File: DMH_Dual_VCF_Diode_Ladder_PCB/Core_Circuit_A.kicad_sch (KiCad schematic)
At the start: 53 parts, among them SW1 SW_SPDT, SW2 SW_SPDT, SW3 SW_SPDT, SW5 Switch_SP3T_APEM5244, U1 TL074, U2 TL074

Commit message: Schematic design in progress
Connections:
- net GND: no longer SW5.3

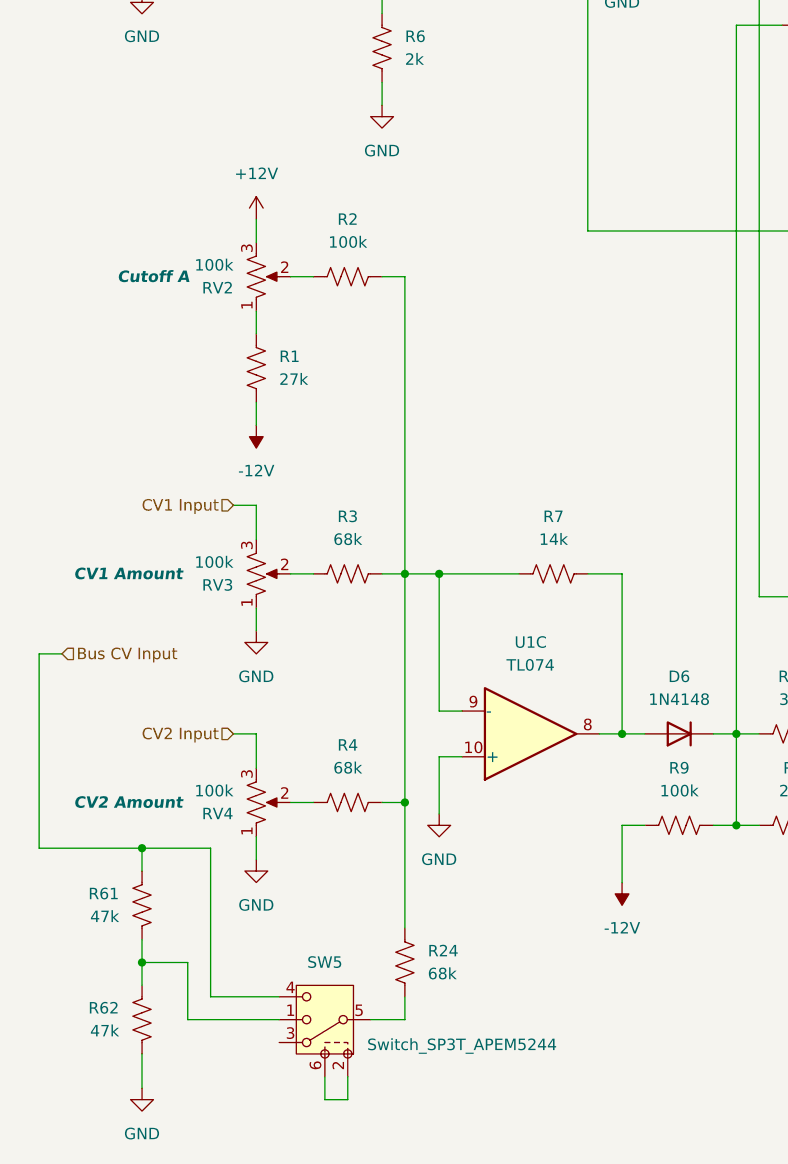
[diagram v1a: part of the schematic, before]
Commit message: Made CV processing page
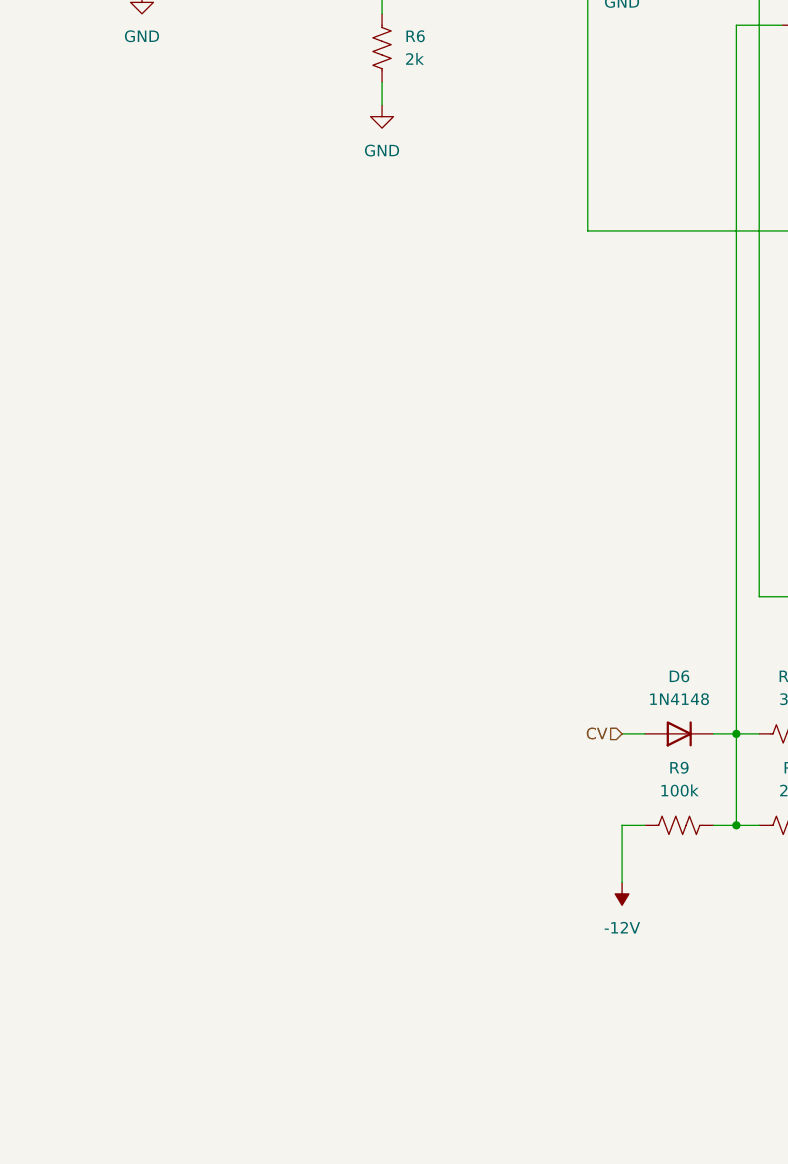
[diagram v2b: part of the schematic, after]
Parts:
- removed R1: 27k, Resistor_THT:R_Axial_DIN0207_L6.3mm_D2.5mm_P7.62mm_Horizontal, symbol Device:R_US
- removed R2: 100k, Resistor_THT:R_Axial_DIN0207_L6.3mm_D2.5mm_P7.62mm_Horizontal, symbol Device:R_US
- removed R24, R3, R4: 68k, Resistor_THT:R_Axial_DIN0207_L6.3mm_D2.5mm_P7.62mm_Horizontal, symbol Device:R_US
- removed R61, R62: 47k, Resistor_THT:R_Axial_DIN0207_L6.3mm_D2.5mm_P7.62mm_Horizontal, symbol Device:R_US
- removed R7: 14k, Resistor_THT:R_Axial_DIN0207_L6.3mm_D2.5mm_P7.62mm_Horizontal, symbol Device:R_US
- removed RV2: 100k, SynthStuff:Potentiometer_Alpha_RD901F-40-00D_Single_Vertical, symbol Device:R_Potentiometer_US
- removed RV3, RV4: 100k, SynthStuff:Potentiometer_TT_P110KH1, symbol Device:R_Potentiometer_US
- removed SW5: Switch_SP3T_APEM5244, symbol SynthStuff:Switch_SP3T
- removed unit 3 of U1
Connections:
- net CV: now reaches D6.2 (A)

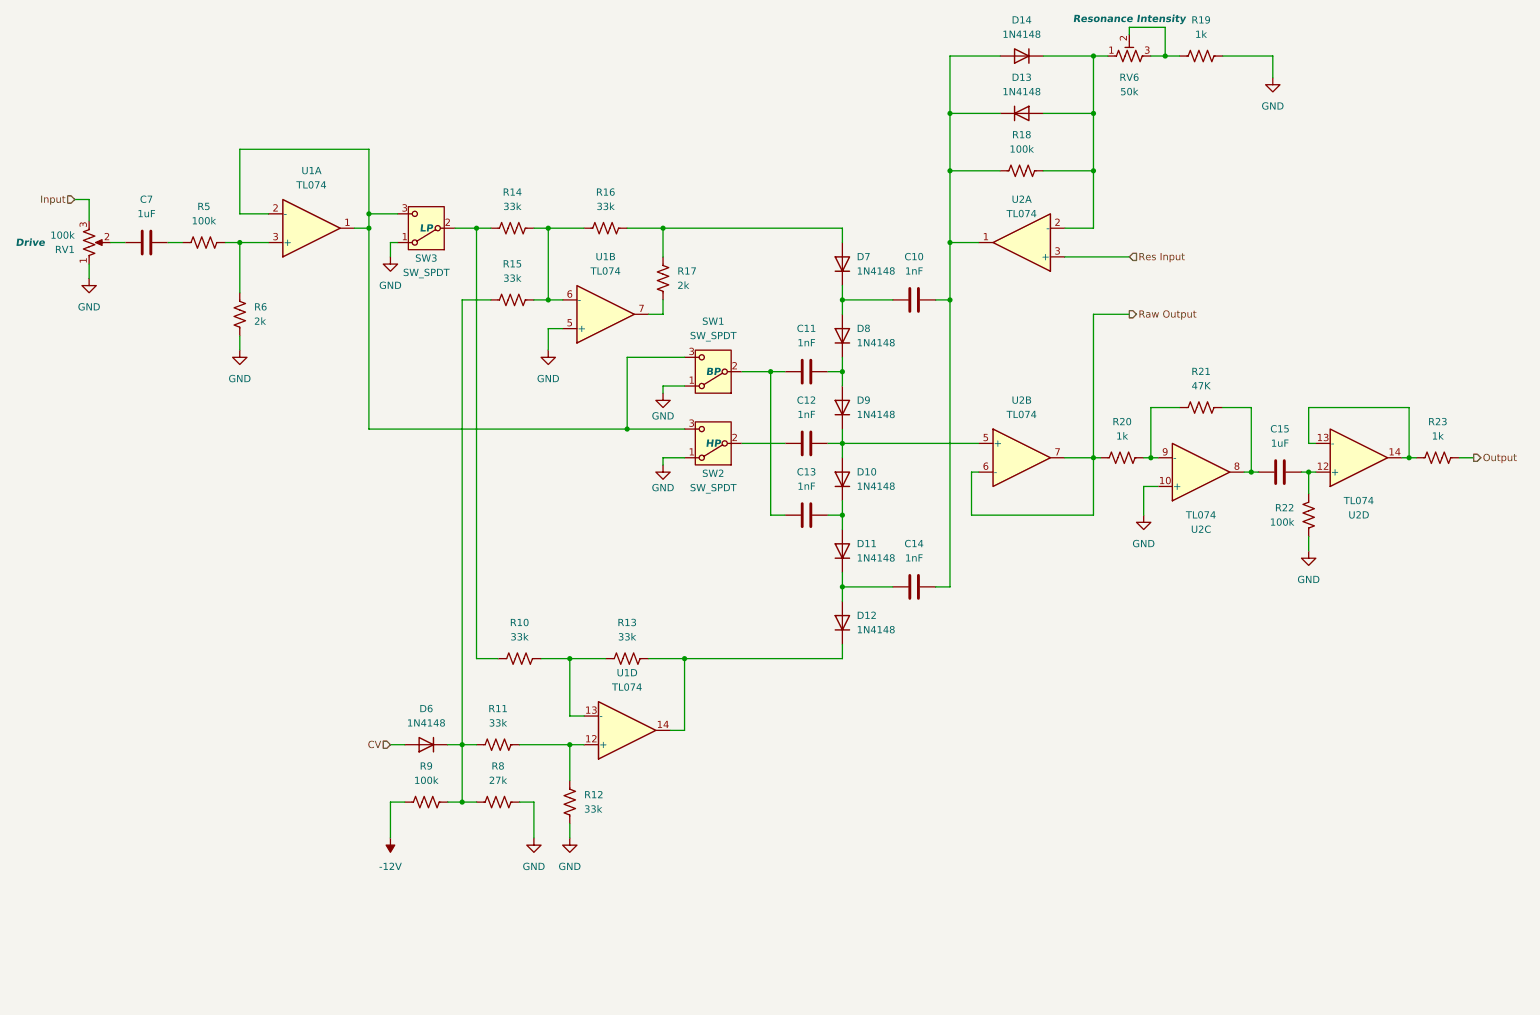
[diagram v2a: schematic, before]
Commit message: Reannotated whole schematic
OpAmp annotation is still tentative.
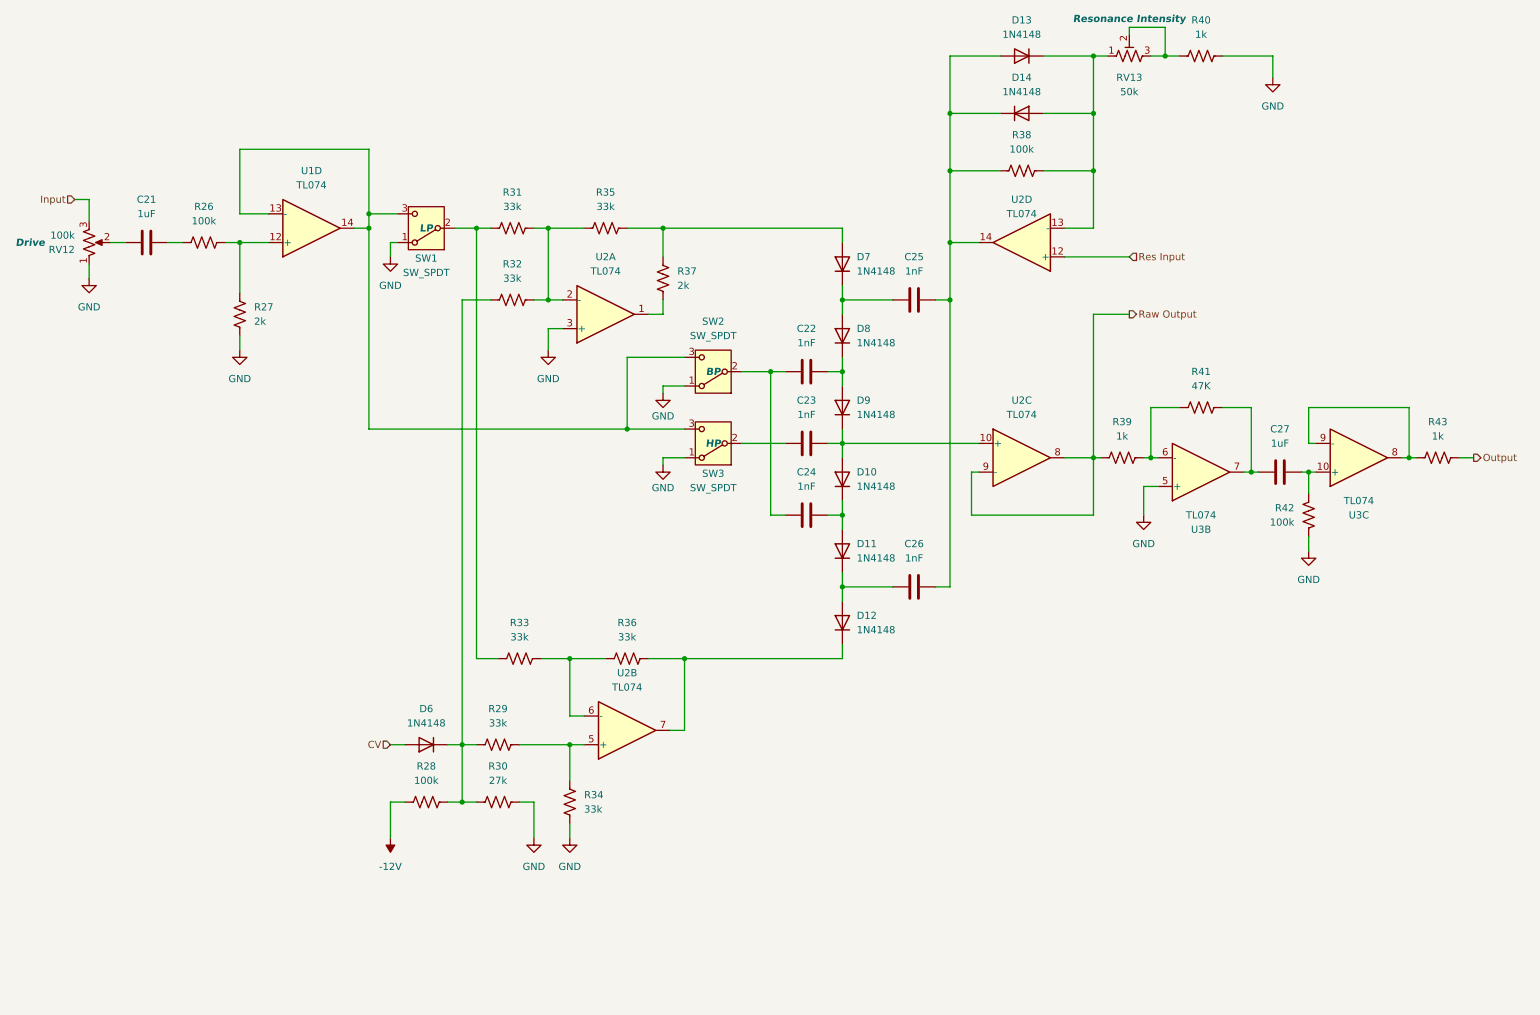
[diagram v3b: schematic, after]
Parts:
- removed C10, C11, C12, C13, C14: 1nF, Capacitor_THT:C_Disc_D4.3mm_W1.9mm_P5.00mm, symbol Device:C
- removed C15, C7: 1uF, Capacitor_THT:C_Disc_D4.3mm_W1.9mm_P5.00mm, symbol Device:C
- removed R10, R11, R12, R13, R14, R15, R16: 33k, Resistor_THT:R_Axial_DIN0207_L6.3mm_D2.5mm_P7.62mm_Horizontal, symbol Device:R_US
- removed R17, R6: 2k, Resistor_THT:R_Axial_DIN0207_L6.3mm_D2.5mm_P7.62mm_Horizontal, symbol Device:R_US
- removed R18, R22, R5, R9: 100k, Resistor_THT:R_Axial_DIN0207_L6.3mm_D2.5mm_P7.62mm_Horizontal, symbol Device:R_US
- removed R19, R20, R23: 1k, Resistor_THT:R_Axial_DIN0207_L6.3mm_D2.5mm_P7.62mm_Horizontal, symbol Device:R_US
- removed R21: 47K, Resistor_THT:R_Axial_DIN0207_L6.3mm_D2.5mm_P7.62mm_Horizontal, symbol Device:R_US
- removed R8: 27k, Resistor_THT:R_Axial_DIN0207_L6.3mm_D2.5mm_P7.62mm_Horizontal, symbol Device:R_US
- removed RV1: 100k, SynthStuff:Potentiometer_Alpha_RD901F-40-00D_Single_Vertical, symbol Device:R_Potentiometer_US
- removed RV6: 50k, Potentiometer_THT:Potentiometer_Bourns_3296W_Vertical, symbol Device:R_Potentiometer_Trim_US
- removed unit 2 of U1
- removed unit 1 of U1
- added C21, C27: 1uF, Capacitor_THT:C_Disc_D4.3mm_W1.9mm_P5.00mm, symbol Device:C
- added C22, C23, C24, C25, C26: 1nF, Capacitor_THT:C_Disc_D4.3mm_W1.9mm_P5.00mm, symbol Device:C
- added R26, R28, R38, R42: 100k, Resistor_THT:R_Axial_DIN0207_L6.3mm_D2.5mm_P7.62mm_Horizontal, symbol Device:R_US
- added R27, R37: 2k, Resistor_THT:R_Axial_DIN0207_L6.3mm_D2.5mm_P7.62mm_Horizontal, symbol Device:R_US
- added R29, R31, R32, R33, R34, R35, R36: 33k, Resistor_THT:R_Axial_DIN0207_L6.3mm_D2.5mm_P7.62mm_Horizontal, symbol Device:R_US
- added R30: 27k, Resistor_THT:R_Axial_DIN0207_L6.3mm_D2.5mm_P7.62mm_Horizontal, symbol Device:R_US
- added R39, R40, R43: 1k, Resistor_THT:R_Axial_DIN0207_L6.3mm_D2.5mm_P7.62mm_Horizontal, symbol Device:R_US
- added R41: 47K, Resistor_THT:R_Axial_DIN0207_L6.3mm_D2.5mm_P7.62mm_Horizontal, symbol Device:R_US
- added RV12: 100k, SynthStuff:Potentiometer_Alpha_RD901F-40-00D_Single_Vertical, symbol Device:R_Potentiometer_US
- added RV13: 50k, Potentiometer_THT:Potentiometer_Bourns_3296W_Vertical, symbol Device:R_Potentiometer_Trim_US
- added U3: TL074, Package_DIP:DIP-14_W7.62mm_Socket, symbol Amplifier_Operational:TL074
- SW1: Function BP -> LP
- SW2: Function HP -> BP
- SW3: Function LP -> HP
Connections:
- net -12V: now also R28.1
- net GND: now also U2.3 (+), R27.1, R30.2, R34.1, R40.2, R42.1, RV12.1, U3.5 (+); no longer U2.10 (+)
- net Input: now also RV12.3
- net Output: now also R43.2
- net Raw Output: now also U2.8, U2.9 (-), R39.1; no longer U2.6 (-), U2.7
- net Res Input: now also U2.12 (+); no longer U2.3 (+)
- net at D6.1 (K): now also R28.2, R29.1, R30.1, R32.1
- net at SW2.2 (B): now also C22.1, C24.1
- net at D10.2 (A), D9.1 (K): now also U2.10 (+), C23.2; no longer U2.5 (+)
- net at D7.2 (A): now also R35.2, R37.2
- net at SW1.2 (B): now also R31.1, R33.1
- net at D10.1 (K), D11.2 (A): now also C24.2
- net at D8.1 (K), D9.2 (A): now also C22.2
- net at SW1.3 (C), SW2.3 (C), SW3.3 (C): now also U1.13 (-), U1.14
- net at D7.1 (K), D8.2 (A): now also C25.1
- net at D13.1 (K), D14.2 (A): now also U2.13 (-), R38.2, RV13.1; no longer U2.1
- net at D13.2 (A), D14.1 (K): now also U2.14, C25.2, C26.2, R38.1; no longer U2.2 (-)
- net at SW3.2 (B): now also C23.1
- net at U1.12 (+): now also R26.2, R27.2
- net at D11.1 (K), D12.2 (A): now also C26.1
- net at D12.1 (K): now also U2.7, R36.2; no longer U1.14
- new net: C21.1, RV12.2
- new net: C27.2, R42.2, U3.10 (+)
- new net: R43.1, U3.8, U3.9 (-)
- new net: C27.1, R41.2, U3.7
- new net: R39.2, R41.1, U3.6 (-)
- new net: R31.2, R32.2, R35.1, U2.2 (-)
- new net: R37.1, U2.1
- new net: R29.2, R34.2, U2.5 (+)
- new net: C21.2, R26.1
- new net: R40.1, RV13.2, RV13.3
- new net: R33.2, R36.1, U2.6 (-)

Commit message: Reannotated OpAmps and cleared errors
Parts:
- renumbered U2 to U3, U3 to U4, U2 to U4
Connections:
- net GND: now also U4.3 (+); no longer U4.5 (+)
- net at C27.2, R42.2: now also U3.5 (+); no longer U3.10 (+)
- net at C27.1, R41.2: now also U4.1; no longer U4.7
- net at R39.2, R41.1: now also U4.2 (-); no longer U4.6 (-)
- new net: R43.1, U3.6 (-), U3.7
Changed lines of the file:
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@@
 		(at 250.19 101.6 0)
 		(mirror x)
-		(unit 3)
+		(unit 2)
 		(exclude_from_sim no)
 		(in_bom yes)
@@
 				(path "/58f4306d-5387-4983-bb08-41a2313fd315/7ad2d702-dfb7-4d49-a82d-34430dd5948f"
 					(reference "U3")
-					(unit 3)
+					(unit 2)
 				)
 			)
@@
 		(at 222.25 104.14 0)
 		(mirror x)
-		(unit 2)
+		(unit 1)
 		(exclude_from_sim no)
 		(in_bom yes)
 		(on_board yes)
 		(dnp no)
-		(property "Reference" "U3"
+		(property "Reference" "U4"
 			(at 222.25 114.3 0)
 			(effects
@@
 			(project "DMH_Dual_VCF_Diode_Ladder_PCB"
 				(path "/58f4306d-5387-4983-bb08-41a2313fd315/7ad2d702-dfb7-4d49-a82d-34430dd5948f"
-					(reference "U3")
-					(unit 2)
+					(reference "U4")
+					(unit 1)
 				)
 			)
@@
 		(dnp no)
 		(fields_autoplaced yes)
-		(property "Reference" "U2"
+		(property "Reference" "U3"
 			(at 116.84 66.04 0)
 			(effects
@@
 			(project "DMH_Dual_VCF_Diode_Ladder_PCB"
 				(path "/58f4306d-5387-4983-bb08-41a2313fd315/7ad2d702-dfb7-4d49-a82d-34430dd5948f"
-					(reference "U2")
+					(reference "U3")
 					(unit 1)
 				)
@@
 		(dnp no)
 		(fields_autoplaced yes)
-		(property "Reference" "U2"
+		(property "Reference" "U4"
 			(at 120.65 139.7 0)
 			(effects
@@
 			(project "DMH_Dual_VCF_Diode_Ladder_PCB"
 				(path "/58f4306d-5387-4983-bb08-41a2313fd315/7ad2d702-dfb7-4d49-a82d-34430dd5948f"
-					(reference "U2")
+					(reference "U4")
 					(unit 2)
 				)
@@
 		(dnp no)
 		(fields_autoplaced yes)
-		(property "Reference" "U2"
+		(property "Reference" "U3"
 			(at 190.5 91.44 0)
 			(effects
@@
 			(project "DMH_Dual_VCF_Diode_Ladder_PCB"
 				(path "/58f4306d-5387-4983-bb08-41a2313fd315/7ad2d702-dfb7-4d49-a82d-34430dd5948f"
-					(reference "U2")
+					(reference "U3")
 					(unit 3)
 				)

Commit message: Updated switches symbols and fps
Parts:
- SW1, SW2, SW3: footprint SynthStuff:Toggle_Switch_THT -> SynthStuff:Toggle_Switch_TE
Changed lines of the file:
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@@
 			)
 		)
-		(property "Footprint" "SynthStuff:Toggle_Switch_THT"
+		(property "Footprint" "SynthStuff:Toggle_Switch_TE"
 			(at 135.89 86.36 0)
 			(effects
@@
 			)
 		)
-		(property "Footprint" "SynthStuff:Toggle_Switch_THT"
+		(property "Footprint" "SynthStuff:Toggle_Switch_TE"
 			(at 85.09 60.96 0)
 			(effects
@@
 			)
 		)
-		(property "Footprint" "SynthStuff:Toggle_Switch_THT"
+		(property "Footprint" "SynthStuff:Toggle_Switch_TE"
 			(at 135.89 99.06 0)
 			(effects

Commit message: Re-annotated OpAmps as per PCB layout
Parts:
- renumbered U4 to U3, U2 to U3, U1 to U5, U3 to U5, U4 to U5
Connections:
- net GND: now also U3.10 (+), U5.10 (+); no longer U3.3 (+), U5.3 (+)
- net Raw Output: now also U3.6 (-), U3.7; no longer U3.8, U3.9 (-)
- net Res Input: now also U3.3 (+); no longer U3.12 (+)
- net at C27.2, R42.2: now also U3.12 (+); no longer U3.5 (+)
- net at C27.1, R41.2: now also U3.8; no longer U3.1
- net at R39.2, R41.1: now also U3.9 (-); no longer U3.2 (-)
- net at R31.2, R32.2, R35.1: now also U5.9 (-); no longer U5.2 (-)
- net at R37.1: now also U5.8; no longer U5.1
- net at C23.2, D10.2 (A), D9.1 (K): now also U3.5 (+); no longer U3.10 (+)
- net at D13.1 (K), D14.2 (A), R38.2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: now also U3.2 (-); no longer U3.13 (-)
- net at C25.2, C26.2, D13.2 (A)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: now also U3.1; no longer U3.14
- net at R29.2, R34.2: now also U5.3 (+); no longer U5.5 (+)
- net at R33.2, R36.1: now also U5.2 (-); no longer U5.6 (-)
- net at D12.1 (K), R36.2: now also U5.1; no longer U5.7
- new net: R43.1, U3.13 (-), U3.14
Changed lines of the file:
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@@
 		(at 250.19 101.6 0)
 		(mirror x)
-		(unit 2)
+		(unit 4)
 		(exclude_from_sim no)
 		(in_bom yes)
@@
 				(path "/58f4306d-5387-4983-bb08-41a2313fd315/7ad2d702-dfb7-4d49-a82d-34430dd5948f"
 					(reference "U3")
-					(unit 2)
+					(unit 4)
 				)
 			)
@@
 		(dnp no)
 		(fields_autoplaced yes)
-		(property "Reference" "U1"
+		(property "Reference" "U5"
 			(at 64.77 50.8 0)
 			(effects
@@
 			(project "DMH_Dual_VCF_Diode_Ladder_PCB"
 				(path "/58f4306d-5387-4983-bb08-41a2313fd315/7ad2d702-dfb7-4d49-a82d-34430dd5948f"
-					(reference "U1")
+					(reference "U5")
 					(unit 4)
 				)
@@
 		(at 222.25 104.14 0)
 		(mirror x)
-		(unit 1)
+		(unit 3)
 		(exclude_from_sim no)
 		(in_bom yes)
 		(on_board yes)
 		(dnp no)
-		(property "Reference" "U4"
+		(property "Reference" "U3"
 			(at 222.25 114.3 0)
 			(effects
@@
 			(project "DMH_Dual_VCF_Diode_Ladder_PCB"
 				(path "/58f4306d-5387-4983-bb08-41a2313fd315/7ad2d702-dfb7-4d49-a82d-34430dd5948f"
-					(reference "U4")
-					(unit 1)
+					(reference "U3")
+					(unit 3)
 				)
 			)
@@
 		(at 116.84 76.2 0)
 		(mirror x)
-		(unit 1)
+		(unit 3)
 		(exclude_from_sim no)
 		(in_bom yes)
@@
 		(dnp no)
 		(fields_autoplaced yes)
-		(property "Reference" "U3"
+		(property "Reference" "U5"
 			(at 116.84 66.04 0)
 			(effects
@@
 			(project "DMH_Dual_VCF_Diode_Ladder_PCB"
 				(path "/58f4306d-5387-4983-bb08-41a2313fd315/7ad2d702-dfb7-4d49-a82d-34430dd5948f"
-					(reference "U3")
-					(unit 1)
+					(reference "U5")
+					(unit 3)
 				)
 			)
@@
 		(lib_id "Amplifier_Operational:TL074")
 		(at 190.5 63.5 180)
-		(unit 4)
+		(unit 1)
 		(exclude_from_sim no)
 		(in_bom yes)
 		(on_board yes)
 		(dnp no)
-		(property "Reference" "U2"
+		(property "Reference" "U3"
 			(at 190.5 55.88 0)
 			(effects
@@
 			(project "DMH_Dual_VCF_Diode_Ladder_PCB"
 				(path "/58f4306d-5387-4983-bb08-41a2313fd315/7ad2d702-dfb7-4d49-a82d-34430dd5948f"
-					(reference "U2")
-					(unit 4)
+					(reference "U3")
+					(unit 1)
 				)
 			)
@@
 		(at 120.65 149.86 0)
 		(mirror x)
-		(unit 2)
+		(unit 1)
 		(exclude_from_sim no)
 		(in_bom yes)
@@
 		(dnp no)
 		(fields_autoplaced yes)
-		(property "Reference" "U4"
+		(property "Reference" "U5"
 			(at 120.65 139.7 0)
 			(effects
@@
 			(project "DMH_Dual_VCF_Diode_Ladder_PCB"
 				(path "/58f4306d-5387-4983-bb08-41a2313fd315/7ad2d702-dfb7-4d49-a82d-34430dd5948f"
-					(reference "U4")
-					(unit 2)
+					(reference "U5")
+					(unit 1)
 				)
 			)
@@
 		(lib_id "Amplifier_Operational:TL074")
 		(at 190.5 101.6 0)
-		(unit 3)
+		(unit 2)
 		(exclude_from_sim no)
 		(in_bom yes)
@@
 				(path "/58f4306d-5387-4983-bb08-41a2313fd315/7ad2d702-dfb7-4d49-a82d-34430dd5948f"
 					(reference "U3")
-					(unit 3)
+					(unit 2)
 				)
 			)
